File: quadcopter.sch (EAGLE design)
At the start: 69 parts, among them J1 AVR_SPI_PRG_6NS, Q1 2.6A, Q2 2.6A, Q3 2.6A, Q4 2.6A, U1 ATMEGA128RFA1, U2 IMU_LSM9DS1TR, Y1 16MHz

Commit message: Board ready for final review
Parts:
- removed D10: Green, LEDs:LED_OVS5MXBCR4GREEN
- removed D9: Blue, LEDs:LED_OVS5MXBCR4BLUE
- removed R11, R5: 100, quadparts_prebuilt:RESISTOR_SMD-2012-0805-100
- added Q5, Q6: 2.6A, quadparts_connie:N_MOSFET_SI2302CDS_T1_E3
- added SW1: PUSHBUTTON_SMD-VERTICAL, quadparts_prebuilt:PUSHBUTTON_SMD-VERTICAL
- D1, D2, D3, D4: value (none) -> 360mV; device quadparts_prebuilt:DIODE-SCHOTTKY_SMD-SOD123 -> quadparts_prebuilt:DIODE-SCHOTTKY_SMD-SOD123-360MV
- R10, R9: value 100 -> 11; device quadparts_prebuilt:RESISTOR_SMD-2012-0805-100 -> quadparts_prebuilt:RESISTOR_SMD-2012-0805-11
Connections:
- removed net N$11: J1.3
- removed net N$12: J1.5
- removed net N$18: D9.A, R9.2
- removed net N$19: D10.A, R5.1
- removed net N$20: R5.2, U1.PG0(DIG3)
- removed net N$26: R9.1, U1.PG1(DIG1)
- removed net N$28: D6.A, R11.1
- removed net N$6 (its old number): JP2.2
- removed net N$7: JP2.3
- removed net N$8: J1.1
- removed net N$9: J1.4
- new net PB6: Q5.G, U1.PB6(OC1B/PCINT6)
- new net PB7: Q6.G, U1.PB7(OC0A/OC1C/PCINT7)
- net BAT_GND: now also Q5.S, Q6.S; no longer D5.C, D6.C
- net GND: now also SW1.2; no longer D10.C, D9.C
- net MISO: now also J1.1
- net MOSI: now also J1.4
- net N$2: now also D6.C, Q5.D; no longer JP1.3
- net N$3: now also D6.A, R9.2; no longer JP1.2
- net N$4: now also D5.C, Q6.D; no longer C1.2
- net RESET: now also C1.2, J1.5, SW1.1
- net RX0: now also JP1.3
- net RX1: now also JP2.3
- net SCK: now also J1.3
- net TX0: now also JP1.2
- net TX1: now also JP2.2
- net VBAT: now also R9.1; no longer R11.2
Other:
- note added: "LEDs"
- note added: "Motor Drivers"
- note added: "Power"
- note added: "Reset Button"
- moved on the sheet: BATT1, C1, C10, C11, C16, C17, C2, C4, C5, C7, C8, D1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

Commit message: Fixed new board errors
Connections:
- removed net N$36: R12.2, U2.SDA/SDI/SDO
- net SDA: now also R12.2, U2.SDA/SDI/SDO
- net VBAT: now also U$3.EN
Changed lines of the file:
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@@
 <pinref part="R10" gate="G$1" pin="1"/>
+</segment>
+<segment>
+<pinref part="U$3" gate="G$1" pin="EN"/>
+<wire x1="-144.78" y1="17.78" x2="-147.32" y2="17.78" width="0.1524" layer="91"/>
+<label x="-152.4" y="17.78" size="1.778" layer="95"/>
 </segment>
 </net>
@@
 <label x="-91.44" y="0" size="1.778" layer="95"/>
 </segment>
+<segment>
+<pinref part="U2" gate="G$1" pin="SDA/SDI/SDO"/>
+<pinref part="R12" gate="G$1" pin="2"/>
+<wire x1="40.64" y1="-111.76" x2="30.48" y2="-111.76" width="0.1524" layer="91"/>
+<label x="30.48" y="-114.3" size="1.778" layer="95"/>
+</segment>
 </net>
 <net name="SCL" class="0">
@@
 </segment>
 </net>
-<net name="N$36" class="0">
-<segment>
-<pinref part="U2" gate="G$1" pin="SDA/SDI/SDO"/>
-<pinref part="R12" gate="G$1" pin="2"/>
-<wire x1="40.64" y1="-111.76" x2="30.48" y2="-111.76" width="0.1524" layer="91"/>
-</segment>
-</net>
 <net name="PB6" class="0">
 <segment>
@@
 </segment>
 </net>
-<net name="N$2" class="0">
+<net name="N$2" class="2">
 <segment>
 <pinref part="D6" gate="G$1" pin="C"/>
@@
 </segment>
 </net>
-<net name="N$3" class="0">
+<net name="N$3" class="2">
 <segment>
 <pinref part="D6" gate="G$1" pin="A"/>
@@
 </segment>
 </net>
-<net name="N$4" class="0">
+<net name="N$4" class="2">
 <segment>
 <pinref part="Q6" gate="G$1" pin="D"/>
@@
 </segment>
 </net>
-<net name="N$6" class="0">
+<net name="N$6" class="2">
 <segment>
 <wire x1="-22.86" y1="132.08" x2="-22.86" y2="137.16" width="0.1524" layer="91"/>

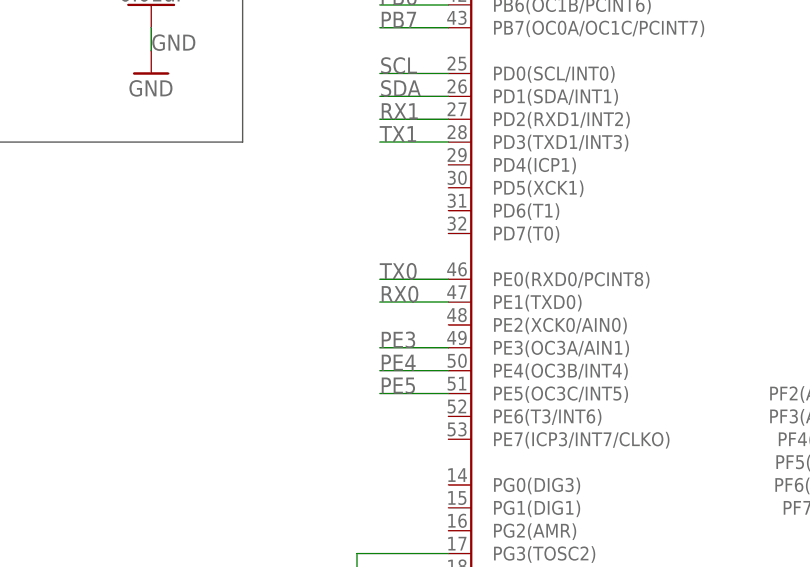
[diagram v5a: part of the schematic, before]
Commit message: more board fixes
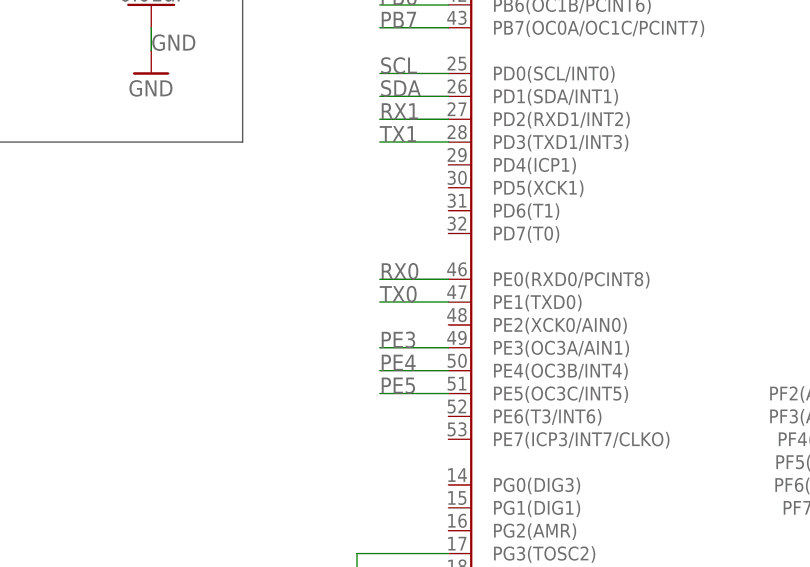
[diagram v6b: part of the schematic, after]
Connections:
- net RX0: now also U1.PE0(RXD0/PCINT8); no longer U1.PE1(TXD0)
- net TX0: now also U1.PE1(TXD0); no longer U1.PE0(RXD0/PCINT8)
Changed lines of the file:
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@@
 <net name="RX0" class="0">
-<segment>
-<pinref part="U1" gate="G$1" pin="PE1(TXD0)"/>
-<wire x1="-83.82" y1="-22.86" x2="-91.44" y2="-22.86" width="0.1524" layer="91"/>
-<label x="-91.44" y="-22.86" size="1.778" layer="95"/>
-</segment>
 <segment>
 <pinref part="JP1" gate="G$1" pin="3"/>
 <wire x1="119.38" y1="-7.62" x2="124.46" y2="-7.62" width="0.1524" layer="91"/>
 <label x="124.46" y="-7.62" size="1.778" layer="95"/>
+</segment>
+<segment>
+<pinref part="U1" gate="G$1" pin="PE0(RXD0/PCINT8)"/>
+<wire x1="-83.82" y1="-20.32" x2="-91.44" y2="-20.32" width="0.1524" layer="91"/>
+<label x="-91.44" y="-20.32" size="1.778" layer="95"/>
 </segment>
 </net>
@@
 </segment>
 </net>
-<net name="N$23" class="0">
+<net name="N$23" class="2">
 <segment>
 <pinref part="J2" gate="G$1" pin="2"/>
@@
 <net name="TX0" class="0">
 <segment>
-<pinref part="U1" gate="G$1" pin="PE0(RXD0/PCINT8)"/>
-<wire x1="-83.82" y1="-20.32" x2="-91.44" y2="-20.32" width="0.1524" layer="91"/>
-<label x="-91.44" y="-20.32" size="1.778" layer="95"/>
-</segment>
-<segment>
 <pinref part="JP1" gate="G$1" pin="2"/>
 <wire x1="119.38" y1="-5.08" x2="124.46" y2="-5.08" width="0.1524" layer="91"/>
 <label x="124.46" y="-5.08" size="1.778" layer="95"/>
 </segment>
-</net>
+<segment>
+<pinref part="U1" gate="G$1" pin="PE1(TXD0)"/>
+<wire x1="-83.82" y1="-22.86" x2="-91.44" y2="-22.86" width="0.1524" layer="91"/>
+<label x="-91.44" y="-22.86" size="1.778" layer="95"/>
+</segment>
+</net>
